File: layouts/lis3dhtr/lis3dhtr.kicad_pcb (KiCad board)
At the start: 2 copper layers, 3 parts

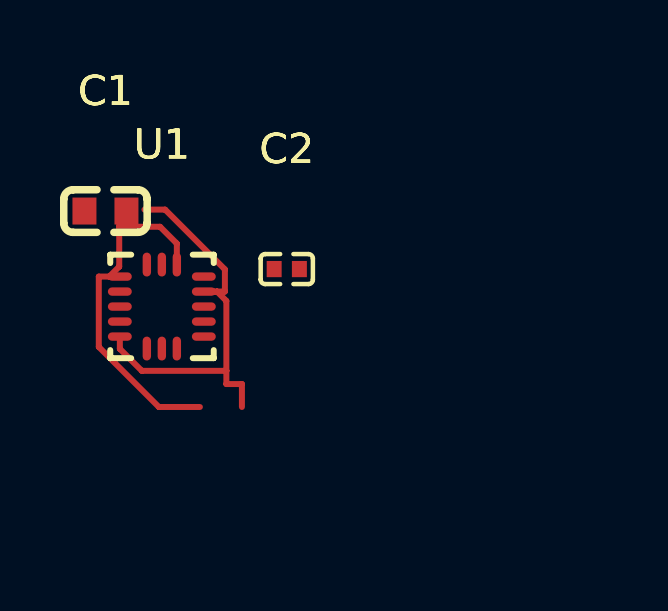
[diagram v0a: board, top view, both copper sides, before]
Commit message: Enhance smart placer with simulated annealing and pre-routing validation
Smart Placer improvements:
- Add simulated annealing refinement (now default) for better wire length optimization
- Add force-directed refinement with improvement safeguard
- Add silkscreen text repositioning to avoid component overlaps
- Significant wire length reductions (e.g., power_filter: 113mm -> 46mm)

Autorouter improvements:
- Add PreRoutingValidator class for pre-flight checks
- Validate unconnected pads, overlapping footprints, unplaced components
- Use pad-based bounds for accurate overlap detection
- Block routing on validation errors with actionable messages

Research:
- Add comprehensive autorouting/autoplacement findings document
- Cover Freerouting Python client, OrthoRoute, DeepPCB, KiCad 9 IPC API
- Document force-directed and simulated annealing algorithms

Cleanup:
- Update .gitignore for DSN/SES files, build artifacts, tools
- Remove stale timestamped build files
- Add parts footprints and symbols

All 10 modules placed and routed successfully.

Co-Authored-By: Claude Opus 4.5 <noreply@anthropic.com>
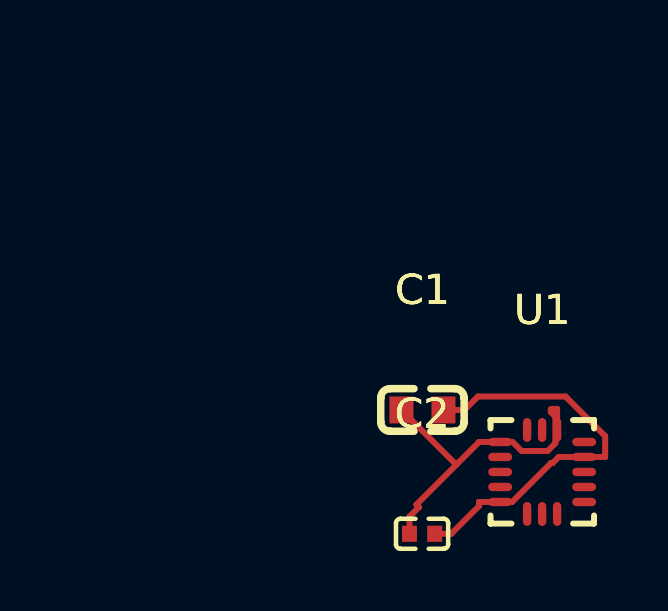
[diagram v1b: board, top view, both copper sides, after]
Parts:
- moved U1 13.8 mm to (112.7, 105.5)
- moved C1 12.5 mm to (108.7, 103.4)
- moved C2 9.91 mm to (108.7, 107.6)
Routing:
- net vcc: track 12.5 -> 11.6 mm
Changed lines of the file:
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@@
 	(footprint "Samsung_Electro_Mechanics_CL05B104KO5NNNC:C0402"
 		(layer "F.Cu")
-		(at 104.165063 98.75)
+		(at 108.6747 107.5734)
 		(property "Reference" "C2"
 			(at 0 -4 0)
@@
 	(footprint "Samsung_Electro_Mechanics_CL10A106KP8NNNC:C0603"
 		(layer "F.Cu")
-		(at 98.120614 96.815959)
+		(at 108.6871 103.4461)
 		(property "Reference" "C1"
 			(at 0 -4 0)
@@
 	(footprint "STMicroelectronics_LIS3DHTR:LGA-16_L3.0-W3.0-P0.50-TL"
 		(layer "F.Cu")
-		(at 100 100)
+		(at 112.6765 105.5133)
 		(property "Reference" "U1"
 			(at 0 -5.4 0)
@@
 	)
 	(segment
-		(start 102.1512 102.5829)
-		(end 102.6696 102.5829)
-		(width 0.2)
-		(layer "F.Cu")
-		(net 8)
-	)
-	(segment
-		(start 102.1512 99.811)
-		(end 102.1512 102.1424)
-		(width 0.2)
-		(layer "F.Cu")
-		(net 8)
-	)
-	(segment
-		(start 98.6 101)
-		(end 98.6 101.4082)
-		(width 0.2)
-		(layer "F.Cu")
-		(net 8)
-	)
-	(segment
-		(start 99.3342 102.1424)
-		(end 102.1512 102.1424)
-		(width 0.2)
-		(layer "F.Cu")
-		(net 8)
-	)
-	(segment
-		(start 102.1512 102.1424)
-		(end 102.1512 102.5829)
-		(width 0.2)
-		(layer "F.Cu")
-		(net 8)
-	)
-	(segment
-		(start 101.4 99.5)
-		(end 101.7509 99.5)
-		(width 0.2)
-		(layer "F.Cu")
-		(net 8)
-	)
-	(segment
-		(start 101.8402 99.5)
-		(end 102.1017 99.5)
-		(width 0.2)
-		(layer "F.Cu")
-		(net 8)
-	)
-	(segment
-		(start 98.6 101.4082)
-		(end 99.3342 102.1424)
-		(width 0.2)
-		(layer "F.Cu")
-		(net 8)
-	)
-	(segment
-		(start 102.6696 102.5829)
-		(end 102.6696 103.3473)
-		(width 0.2)
-		(layer "F.Cu")
-		(net 8)
-	)
-	(segment
-		(start 101.7509 99.5)
-		(end 101.8402 99.5)
-		(width 0.2)
-		(layer "F.Cu")
-		(net 8)
-	)
-	(segment
-		(start 101.8402 99.5)
-		(end 102.1512 99.811)
-		(width 0.2)
-		(layer "F.Cu")
-		(net 8)
-	)
-	(segment
-		(start 102.1017 98.76)
-		(end 100.1096 96.7679)
-		(width 0.2)
-		(layer "F.Cu")
-		(net 8)
-	)
-	(segment
-		(start 102.1017 99.5)
-		(end 102.1017 98.76)
-		(width 0.2)
-		(layer "F.Cu")
-		(net 8)
-	)
-	(segment
-		(start 100.1096 96.7679)
-		(end 99.42 96.7679)
-		(width 0.2)
-		(layer "F.Cu")
-		(net 8)
-	)
-	(segment
-		(start 100.5 98.6)
-		(end 100.5 97.8983)
-		(width 0.2)
-		(layer "F.Cu")
-		(net 14)
-	)
-	(segment
-		(start 98.58 98.6692)
-		(end 98.58 97.3396)
-		(width 0.2)
-		(layer "F.Cu")
-		(net 14)
-	)
-	(segment
-		(start 98.2492 99)
-		(end 97.8983 99)
-		(width 0.2)
-		(layer "F.Cu")
-		(net 14)
-	)
-	(segment
-		(start 99.9009 103.3473)
-		(end 97.8983 101.3447)
-		(width 0.2)
-		(layer "F.Cu")
-		(net 14)
-	)
-	(segment
-		(start 98.58 97.3396)
-		(end 99.9413 97.3396)
-		(width 0.2)
-		(layer "F.Cu")
-		(net 14)
-	)
-	(segment
-		(start 99.9413 97.3396)
-		(end 100.5 97.8983)
-		(width 0.2)
-		(layer "F.Cu")
-		(net 14)
-	)
-	(segment
-		(start 98.58 96.7679)
-		(end 98.58 97.3396)
-		(width 0.2)
-		(layer "F.Cu")
-		(net 14)
-	)
-	(segment
-		(start 98.2492 99)
-		(end 98.58 98.6692)
-		(width 0.2)
-		(layer "F.Cu")
-		(net 14)
-	)
-	(segment
-		(start 97.8983 101.3447)
-		(end 97.8983 99)
-		(width 0.2)
-		(layer "F.Cu")
-		(net 14)
-	)
-	(segment
-		(start 98.6 99)
-		(end 98.2492 99)
-		(width 0.2)
-		(layer "F.Cu")
-		(net 14)
-	)
-	(segment
-		(start 101.2696 103.3473)
-		(end 99.9009 103.3473)
-		(width 0.2)
-		(layer "F.Cu")
+		(start 109.6464 107.5734)
+		(end 110.5748 106.645)
+		(width 0.2)
+		(layer "F.Cu")
+		(net 8)
+	)
+	(segment
+		(start 113.4572 102.9984)
+		(end 114.7782 104.3194)
+		(width 0.2)
+		(layer "F.Cu")
+		(net 8)
+	)
+	(segment
+		(start 114.0765 105.0133)
+		(end 114.7782 105.0133)
+		(width 0.2)
+		(layer "F.Cu")
+		(net 8)
+	)
+	(segment
+		(start 113.0258 105.2167)
+		(end 113.2292 105.0133)
+		(width 0.2)
+		(layer "F.Cu")
+		(net 8)
+	)
+	(segment
+		(start 111.2765 106.5133)
+		(end 111.6765 106.5133)
+		(width 0.2)
+		(layer "F.Cu")
+		(net 8)
+	)
+	(segment
+		(start 110.0888 103.4461)
+		(end 110.5365 102.9984)
+		(width 0.2)
+		(layer "F.Cu")
+		(net 8)
+	)
+	(segment
+		(start 111.2765 106.5133)
+		(end 110.5748 106.5133)
+		(width 0.2)
+		(layer "F.Cu")
+		(net 8)
+	)
+	(segment
+		(start 109.0947 107.5734)
+		(end 109.6464 107.5734)
+		(width 0.2)
+		(layer "F.Cu")
+		(net 8)
+	)
+	(segment
+		(start 111.6765 106.5133)
+		(end 112.9731 105.2167)
+		(width 0.2)
+		(layer "F.Cu")
+		(net 8)
+	)
+	(segment
+		(start 110.5748 106.645)
+		(end 110.5748 106.5133)
+		(width 0.2)
+		(layer "F.Cu")
+		(net 8)
+	)
+	(segment
+		(start 114.7782 104.3194)
+		(end 114.7782 105.0133)
+		(width 0.2)
+		(layer "F.Cu")
+		(net 8)
+	)
+	(segment
+		(start 113.2292 105.0133)
+		(end 114.0765 105.0133)
+		(width 0.2)
+		(layer "F.Cu")
+		(net 8)
+	)
+	(segment
+		(start 110.5365 102.9984)
+		(end 113.4572 102.9984)
+		(width 0.2)
+		(layer "F.Cu")
+		(net 8)
+	)
+	(segment
+		(start 109.3871 103.4461)
+		(end 110.0888 103.4461)
+		(width 0.2)
+		(layer "F.Cu")
+		(net 8)
+	)
+	(segment
+		(start 112.9731 105.2167)
+		(end 113.0258 105.2167)
+		(width 0.2)
+		(layer "F.Cu")
+		(net 8)
+	)
+	(segment
+		(start 112.9654 103.5175)
+		(end 112.9654 103.4349)
+		(width 0.2)
+		(layer "F.Cu")
+		(net 14)
+	)
+	(segment
+		(start 109.8146 105.2735)
+		(end 110.5748 104.5133)
+		(width 0.2)
+		(layer "F.Cu")
+		(net 14)
+	)
+	(segment
+		(start 112.8595 104.815)
+		(end 113.1182 104.5563)
+		(width 0.2)
+		(layer "F.Cu")
+		(net 14)
+	)
+	(segment
+		(start 113.1765 104.1133)
+		(end 113.1765 103.4116)
+		(width 0.2)
+		(layer "F.Cu")
+		(net 14)
+	)
+	(segment
+		(start 113.1182 104.5563)
+		(end 113.1182 103.6703)
+		(width 0.2)
+		(layer "F.Cu")
+		(net 14)
+	)
+	(segment
+		(start 108.2547 107.0017)
+		(end 108.5709 106.6855)
+		(width 0.2)
+		(layer "F.Cu")
+		(net 14)
+	)
+	(segment
+		(start 111.2765 104.5133)
+		(end 110.5748 104.5133)
+		(width 0.2)
+		(layer "F.Cu")
+		(net 14)
+	)
+	(segment
+		(start 108.2547 107.5734)
+		(end 108.2547 107.0017)
+		(width 0.2)
+		(layer "F.Cu")
+		(net 14)
+	)
+	(segment
+		(start 109.8146 105.2735)
+		(end 107.9871 103.4461)
+		(width 0.2)
+		(layer "F.Cu")
+		(net 14)
+	)
+	(segment
+		(start 108.5709 106.6855)
+		(end 108.4868 106.6013)
+		(width 0.2)
+		(layer "F.Cu")
+		(net 14)
+	)
+	(segment
+		(start 113.1182 103.6703)
+		(end 112.9654 103.5175)
+		(width 0.2)
+		(layer "F.Cu")
+		(net 14)
+	)
+	(segment
+		(start 108.4868 106.6013)
+		(end 109.8146 105.2735)
+		(width 0.2)
+		(layer "F.Cu")
+		(net 14)
+	)
+	(segment
+		(start 112.9887 103.4116)
+		(end 113.1765 103.4116)
+		(width 0.2)
+		(layer "F.Cu")
+		(net 14)
+	)
+	(segment
+		(start 111.6918 104.5133)
+		(end 111.9935 104.815)
+		(width 0.2)
+		(layer "F.Cu")
+		(net 14)
+	)
+	(segment
+		(start 111.2765 104.5133)
+		(end 111.6918 104.5133)
+		(width 0.2)
+		(layer "F.Cu")
+		(net 14)
+	)
+	(segment
+		(start 111.9935 104.815)
+		(end 112.8595 104.815)
+		(width 0.2)
+		(layer "F.Cu")
+		(net 14)
+	)
+	(segment
+		(start 112.9654 103.4349)
+		(end 112.9887 103.4116)
+		(width 0.2)
+		(layer "F.Cu")
